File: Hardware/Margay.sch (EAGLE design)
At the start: 70 parts, among them IC1 ATMEGA644M, J1 CONN_42.54_SCREW, J2 CONN_6SCREW_2.54, Q1 FDN360P, Q2 DMG3404, Q3 2N7002, Q4 FDN360P, Q6 FDN360P, U2 FT231X-Q

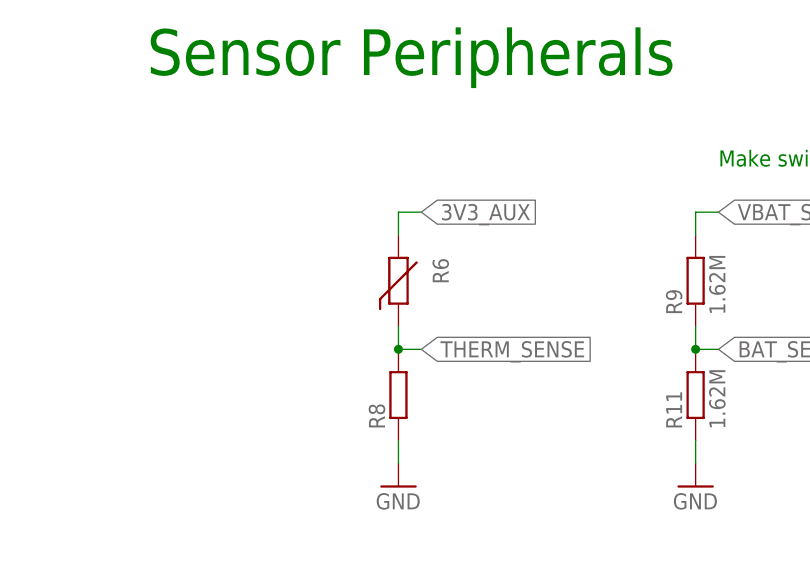
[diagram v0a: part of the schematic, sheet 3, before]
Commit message: Updated test files, pick and place info, and fixed part info
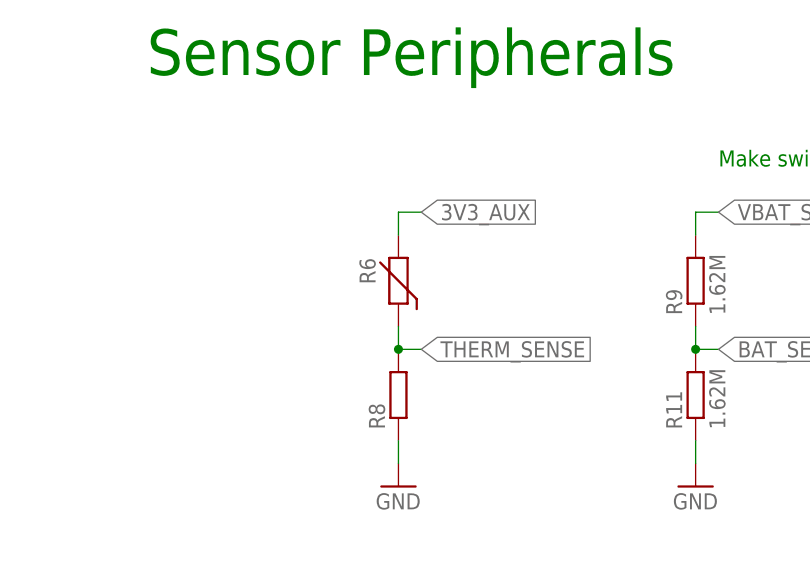
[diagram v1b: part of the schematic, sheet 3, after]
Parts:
- R8: device bschulz:R-EU_R0603 -> bschulz_passives:R-EU_P10KR0603
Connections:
- net 3V3_AUX: now also R6.1; no longer R6.2
- net THERM_SENSE: now also R6.2; no longer R6.1
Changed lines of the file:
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@@
 <grid distance="0.1" unitdist="inch" unit="inch" style="lines" multiple="1" display="no" altdistance="0.01" altunitdist="inch" altunit="inch"/>
 <layers>
-<layer number="1" name="Top" color="4" fill="1" visible="no" active="no"/>
-<layer number="2" name="Route2" color="1" fill="3" visible="no" active="no"/>
-<layer number="3" name="Route3" color="4" fill="3" visible="no" active="no"/>
-<layer number="4" name="Route4" color="1" fill="4" visible="no" active="no"/>
-<layer number="5" name="Route5" color="4" fill="4" visible="no" active="no"/>
-<layer number="6" name="Route6" color="1" fill="8" visible="no" active="no"/>
-<layer number="7" name="Route7" color="4" fill="8" visible="no" active="no"/>
-<layer number="8" name="Route8" color="1" fill="2" visible="no" active="no"/>
-<layer number="9" name="Route9" color="4" fill="2" visible="no" active="no"/>
-<layer number="10" name="Route10" color="1" fill="7" visible="no" active="no"/>
-<layer number="11" name="Route11" color="4" fill="7" visible="no" active="no"/>
-<layer number="12" name="Route12" color="1" fill="5" visible="no" active="no"/>
-<layer number="13" name="Route13" color="4" fill="5" visible="no" active="no"/>
-<layer number="14" name="Route14" color="1" fill="6" visible="no" active="no"/>
-<layer number="15" name="Route15" color="4" fill="6" visible="no" active="no"/>
-<layer number="16" name="Bottom" color="1" fill="1" visible="no" active="no"/>
-<layer number="17" name="Pads" color="2" fill="1" visible="no" active="no"/>
-<layer number="18" name="Vias" color="2" fill="1" visible="no" active="no"/>
-<layer number="19" name="Unrouted" color="6" fill="1" visible="no" active="no"/>
-<layer number="20" name="Dimension" color="24" fill="1" visible="no" active="no"/>
-<layer number="21" name="tPlace" color="7" fill="1" visible="no" active="no"/>
-<layer number="22" name="bPlace" color="7" fill="1" visible="no" active="no"/>
-<layer number="23" name="tOrigins" color="15" fill="1" visible="no" active="no"/>
-<layer number="24" name="bOrigins" color="15" fill="1" visible="no" active="no"/>
-<layer number="25" name="tNames" color="7" fill="1" visible="no" active="no"/>
-<layer number="26" name="bNames" color="7" fill="1" visible="no" active="no"/>
-<layer number="27" name="tValues" color="7" fill="1" visible="no" active="no"/>
-<layer number="28" name="bValues" color="7" fill="1" visible="no" active="no"/>
+<layer number="1" name="Top" color="4" fill="1" visible="yes" active="no"/>
+<layer number="2" name="Route2" color="1" fill="3" visible="yes" active="no"/>
+<layer number="3" name="Route3" color="4" fill="3" visible="yes" active="no"/>
+<layer number="4" name="Route4" color="1" fill="4" visible="yes" active="no"/>
+<layer number="5" name="Route5" color="4" fill="4" visible="yes" active="no"/>
+<layer number="6" name="Route6" color="1" fill="8" visible="yes" active="no"/>
+<layer number="7" name="Route7" color="4" fill="8" visible="yes" active="no"/>
+<layer number="8" name="Route8" color="1" fill="2" visible="yes" active="no"/>
+<layer number="9" name="Route9" color="4" fill="2" visible="yes" active="no"/>
+<layer number="10" name="Route10" color="1" fill="7" visible="yes" active="no"/>
+<layer number="11" name="Route11" color="4" fill="7" visible="yes" active="no"/>
+<layer number="12" name="Route12" color="1" fill="5" visible="yes" active="no"/>
+<layer number="13" name="Route13" color="4" fill="5" visible="yes" active="no"/>
+<layer number="14" name="Route14" color="1" fill="6" visible="yes" active="no"/>
+<layer number="15" name="Route15" color="4" fill="6" visible="yes" active="no"/>
+<layer number="16" name="Bottom" color="1" fill="1" visible="yes" active="no"/>
+<layer number="17" name="Pads" color="2" fill="1" visible="yes" active="no"/>
+<layer number="18" name="Vias" color="2" fill="1" visible="yes" active="no"/>
+<layer number="19" name="Unrouted" color="6" fill="1" visible="yes" active="no"/>
+<layer number="20" name="Dimension" color="24" fill="1" visible="yes" active="no"/>
+<layer number="21" name="tPlace" color="7" fill="1" visible="yes" active="no"/>
+<layer number="22" name="bPlace" color="7" fill="1" visible="yes" active="no"/>
+<layer number="23" name="tOrigins" color="15" fill="1" visible="yes" active="no"/>
+<layer number="24" name="bOrigins" color="15" fill="1" visible="yes" active="no"/>
+<layer number="25" name="tNames" color="7" fill="1" visible="yes" active="no"/>
+<layer number="26" name="bNames" color="7" fill="1" visible="yes" active="no"/>
+<layer number="27" name="tValues" color="7" fill="1" visible="yes" active="no"/>
+<layer number="28" name="bValues" color="7" fill="1" visible="yes" active="no"/>
 <layer number="29" name="tStop" color="7" fill="3" visible="no" active="no"/>
 <layer number="30" name="bStop" color="7" fill="6" visible="no" active="no"/>
@@
 <layer number="35" name="tGlue" color="7" fill="4" visible="no" active="no"/>
 <layer number="36" name="bGlue" color="7" fill="5" visible="no" active="no"/>
-<layer number="37" name="tTest" color="7" fill="1" visible="no" active="no"/>
-<layer number="38" name="bTest" color="7" fill="1" visible="no" active="no"/>
+<layer number="37" name="tTest" color="7" fill="1" visible="yes" active="no"/>
+<layer number="38" name="bTest" color="7" fill="1" visible="yes" active="no"/>
 <layer number="39" name="tKeepout" color="4" fill="11" visible="no" active="no"/>
 <layer number="40" name="bKeepout" color="1" fill="11" visible="no" active="no"/>
@@
 <layer number="44" name="Drills" color="7" fill="1" visible="no" active="no"/>
 <layer number="45" name="Holes" color="7" fill="1" visible="no" active="no"/>
-<layer number="46" name="Milling" color="3" fill="1" visible="no" active="no"/>
-<layer number="47" name="Measures" color="7" fill="1" visible="no" active="no"/>
-<layer number="48" name="Document" color="7" fill="1" visible="no" active="no"/>
-<layer number="49" name="Reference" color="7" fill="1" visible="no" active="no"/>
-<layer number="50" name="dxf" color="7" fill="1" visible="no" active="no"/>
-<layer number="51" name="tDocu" color="7" fill="1" visible="no" active="no"/>
-<layer number="52" name="bDocu" color="7" fill="1" visible="no" active="no"/>
-<layer number="53" name="tGND_GNDA" color="7" fill="9" visible="no" active="no"/>
-<layer number="54" name="bGND_GNDA" color="1" fill="9" visible="no" active="no"/>
-<layer number="56" name="wert" color="7" fill="1" visible="no" active="no"/>
-<layer number="57" name="tCAD" color="7" fill="1" visible="no" active="no"/>
-<layer number="59" name="tCarbon" color="7" fill="1" visible="no" active="no"/>
-<layer number="60" name="bCarbon" color="7" fill="1" visible="no" active="no"/>
+<layer number="46" name="Milling" color="3" fill="1" visible="yes" active="no"/>
+<layer number="47" name="Measures" color="7" fill="1" visible="yes" active="no"/>
+<layer number="48" name="Document" color="7" fill="1" visible="yes" active="no"/>
+<layer number="49" name="Reference" color="7" fill="1" visible="yes" active="no"/>
+<layer number="50" name="dxf" color="7" fill="1" visible="yes" active="no"/>
+<layer number="51" name="tDocu" color="7" fill="1" visible="yes" active="no"/>
+<layer number="52" name="bDocu" color="7" fill="1" visible="yes" active="no"/>
+<layer number="53" name="tGND_GNDA" color="7" fill="9" visible="yes" active="no"/>
+<layer number="54" name="bGND_GNDA" color="1" fill="9" visible="yes" active="no"/>
+<layer number="56" name="wert" color="7" fill="1" visible="yes" active="no"/>
+<layer number="57" name="tCAD" color="7" fill="1" visible="yes" active="no"/>
+<layer number="59" name="tCarbon" color="7" fill="1" visible="yes" active="no"/>
+<layer number="60" name="bCarbon" color="7" fill="1" visible="yes" active="no"/>
 <layer number="88" name="SimResults" color="9" fill="1" visible="yes" active="yes"/>
 <layer number="89" name="SimProbes" color="9" fill="1" visible="yes" active="yes"/>
@@
 <attribute name="MPN" value="NCU18XH103F60RB"/>
 </part>
-<part name="R8" library="bschulz" deviceset="R-EU_" device="R0603">
+<part name="R8" library="bschulz_passives" deviceset="R-EU_" device="R0603" technology="P10K">
 <attribute name="DIGIKEY" value="P10KDBCT-ND "/>
 <attribute name="MF" value="Panasonic"/>
@@
 </instance>
 <instance part="GND9" gate="1" x="228.6" y="88.9"/>
-<instance part="R6" gate="G$1" x="193.04" y="177.8" rot="R270"/>
+<instance part="R6" gate="G$1" x="193.04" y="177.8" rot="MR270"/>
 <instance part="R8" gate="G$1" x="193.04" y="165.1" rot="R90"/>
 <instance part="R9" gate="G$1" x="226.06" y="177.8" rot="R90"/>
@@
 </segment>
 <segment>
-<pinref part="R6" gate="G$1" pin="2"/>
+<pinref part="R6" gate="G$1" pin="1"/>
 <wire x1="193.04" y1="182.88" x2="193.04" y2="185.42" width="0.1524" layer="91"/>
 <wire x1="193.04" y1="185.42" x2="195.58" y2="185.42" width="0.1524" layer="91"/>
@@
 <segment>
 <pinref part="R8" gate="G$1" pin="2"/>
-<pinref part="R6" gate="G$1" pin="1"/>
+<pinref part="R6" gate="G$1" pin="2"/>
 <wire x1="193.04" y1="170.18" x2="193.04" y2="172.72" width="0.1524" layer="91"/>
 <wire x1="193.04" y1="170.18" x2="195.58" y2="170.18" width="0.1524" layer="91"/>

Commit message: Added reference designators and legacy hardware test
Added legacy hardware testing file and reference designator image
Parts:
- C13: device bschulz:C-EU10UFC0805 -> bschulz_passives:C-EU10UFC0805
- C14, C17, C6: device bschulz:C-EU0.1UFC0603 -> bschulz_passives:C-EU0.1UFC0603
- C21: device bschulz:C-EU1UFC0603 -> bschulz_passives:C-EU1UFC0603
- C25, C5: device bschulz_passives:C-EU12PFC0603 -> bschulz_passives:C-EUC0603
- CX2, CX3: device bschulz:C-EU12PFC0603 -> bschulz_passives:C-EU12PFC0603

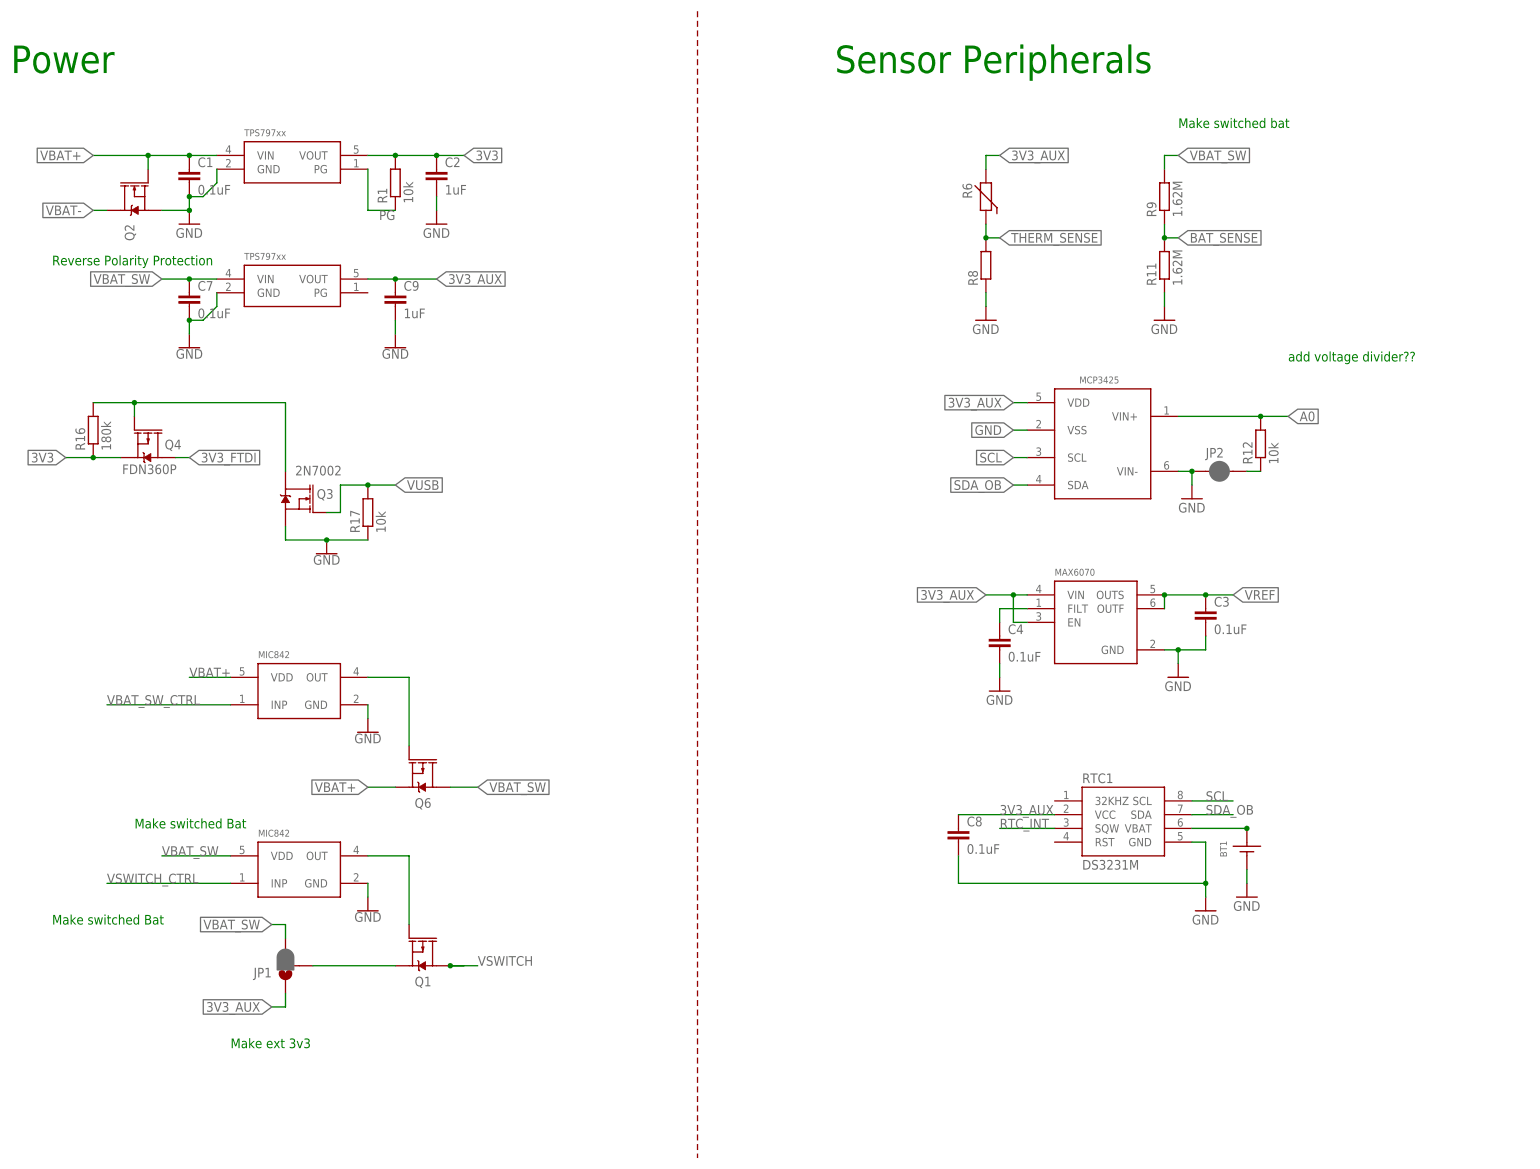
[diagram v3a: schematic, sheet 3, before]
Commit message: Cleaned up schematic, added board and schematic images for v1.0
Added documentation for version 1.0, added schematic PDF, board images, and updated BOM to fix ADC part number
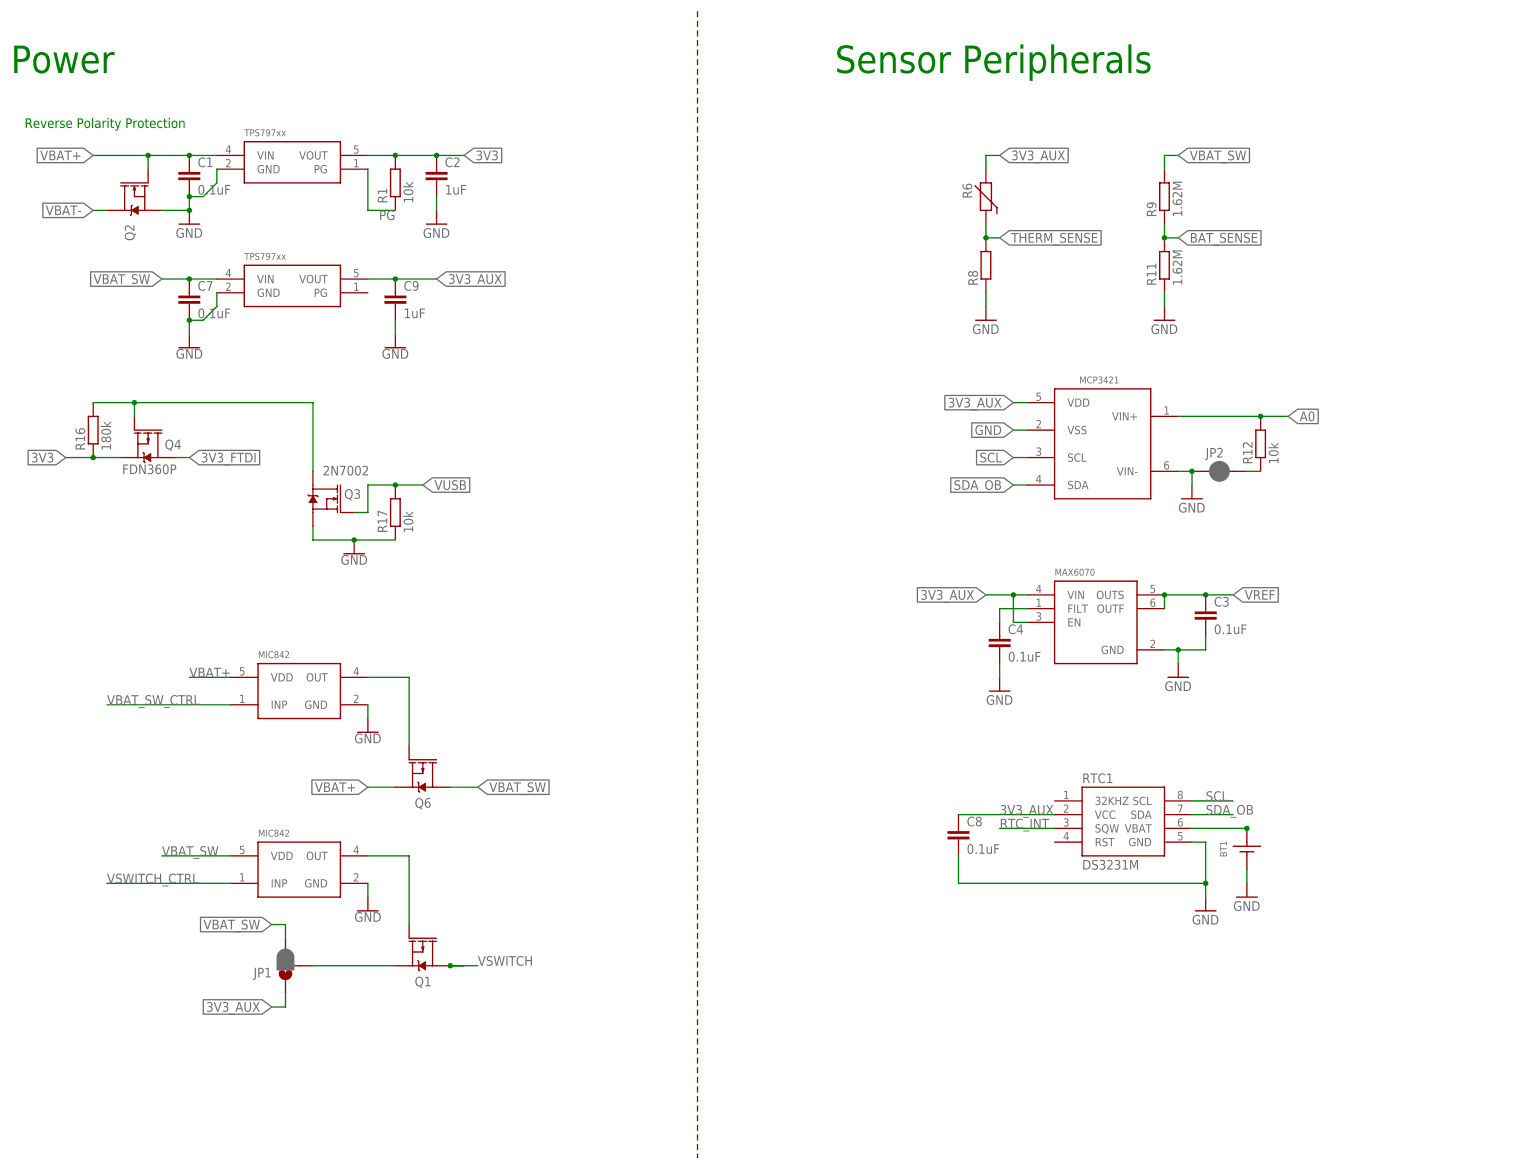
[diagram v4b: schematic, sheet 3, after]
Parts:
- D+, D-: value 27ohm -> 27
- U$8: value MCP3425 -> MCP3421A1; device bschulz:MCP3425 -> bschulz:MCP3421A1
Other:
- note added: "Pin 0"
- note added: "Pin 10"
- note added: "Pin 11"
- note added: "Pin 16"
- note added: "Pin 17"
- note added: "Pin 18"
- note added: "Pin 21"
- note added: "Pin 22"
- note added: "Pin 5"
- note added: "Pin 6"
- note added: "Pin 7"
- note added: "Pin 8"
- note added: "Pin 9"
- note removed: "Check polarity!"
- note removed: "Connect to FTDI isolated 3v3 line"
- note removed: "Make ext 3v3"
- note removed: "Make switched Bat"
- note removed: "Make switched bat"
- note removed: "NOTE: Add LEDs to TX and RX lines?"
- note removed: "NOTE: Connect to MUX (open drain)"
- note removed: "Provide jumper for SDA switch and power switch"
- note removed: "Switch internal SDA line to isolate MCP3425 and to prevent general conflicts!"
- note removed: "add voltage divider??"
- moved on the sheet: Q3, R17
